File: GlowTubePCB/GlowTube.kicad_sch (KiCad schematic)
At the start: 38 parts, among them J1 Conn_01x07, P1 Solder_Pad, P2 Solder_Pad, P3 Solder_Pad, P4 Solder_Pad, P5 Solder_Pad, P6 Solder_Pad, SW1 TS-1185EC-C-D-B, SW2 TS-1185EC-C-D-B, U1 SN74AHCT32QPWRQ1, U2 ESP32-WROOM-32E (4MB), U3 CP2102-GMR, U4 BL1117-33CX, U5 UMH3N, U6 MSM261D4030H1CPM

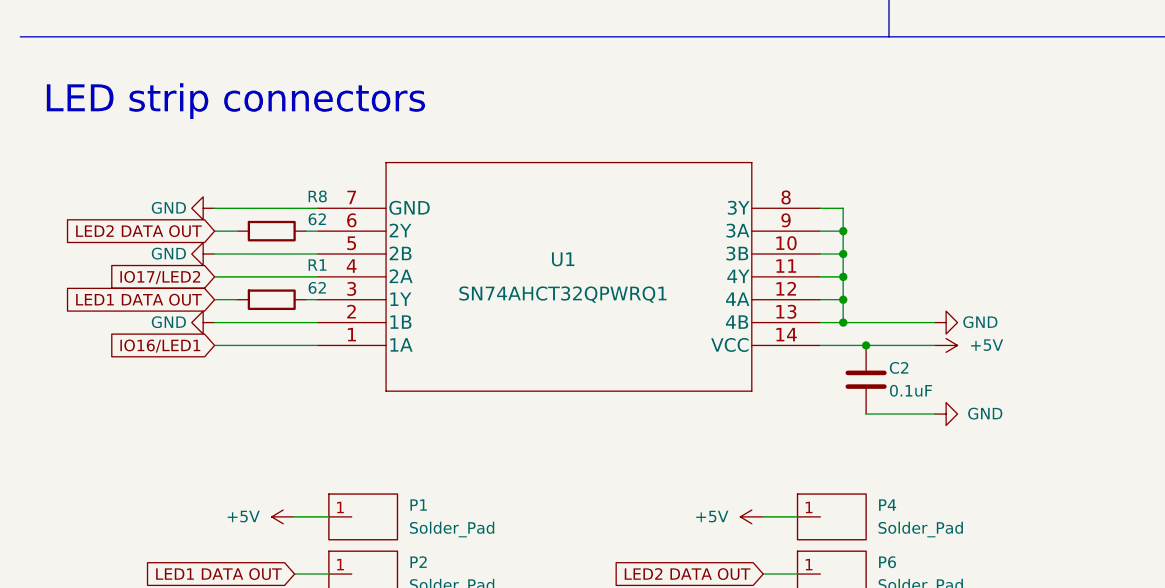
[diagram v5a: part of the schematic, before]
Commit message: replaced microphone and levelshifter
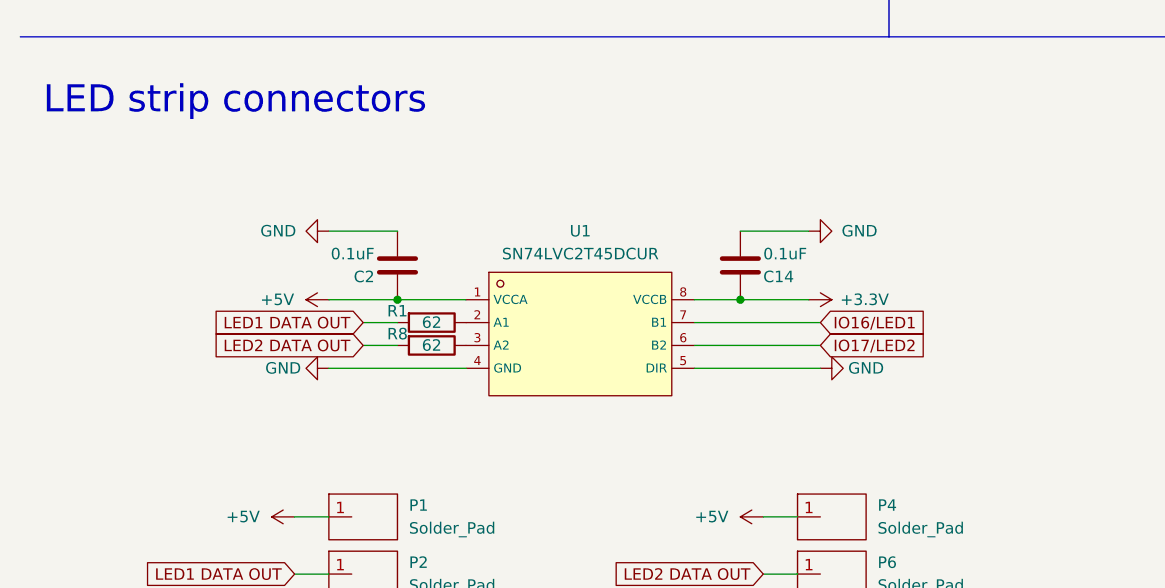
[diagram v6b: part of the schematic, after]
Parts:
- removed U1: SN74AHCT32QPWRQ1, SN74AHCT32QPWRQ1:SN74AHCT32QPWRQ1, symbol SN74AHCT32QPWRQ1:SN74AHCT32QPWRQ1
- added C14: 0.1uF, Capacitor_SMD:C_0603_1608Metric_Pad1.08x0.95mm_HandSolder, symbol Device:C
- added U1: SN74LVC2T45DCUR, footprint:VSSOP-8_L2.4-W2.1-P0.50-LS3.2-BR, symbol MyParts:SN74LVC2T45DCUR
- J1, P1, P2, P3, P4, P5, P6: now left out of the parts list
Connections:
- net +3V3: now also C14.1, U1.8 (VCCB)
- net +5V: now also U1.1 (VCCA)
- net GND: now also C14.2, U1.4 (GND), U1.5 (DIR)
- net IO16/LED1: now also U1.7 (B1)
- net IO17/LED2: now also U1.6 (B2)
- net at R8.1: now also U1.3 (A2)
- net at R1.1: now also U1.2 (A1)

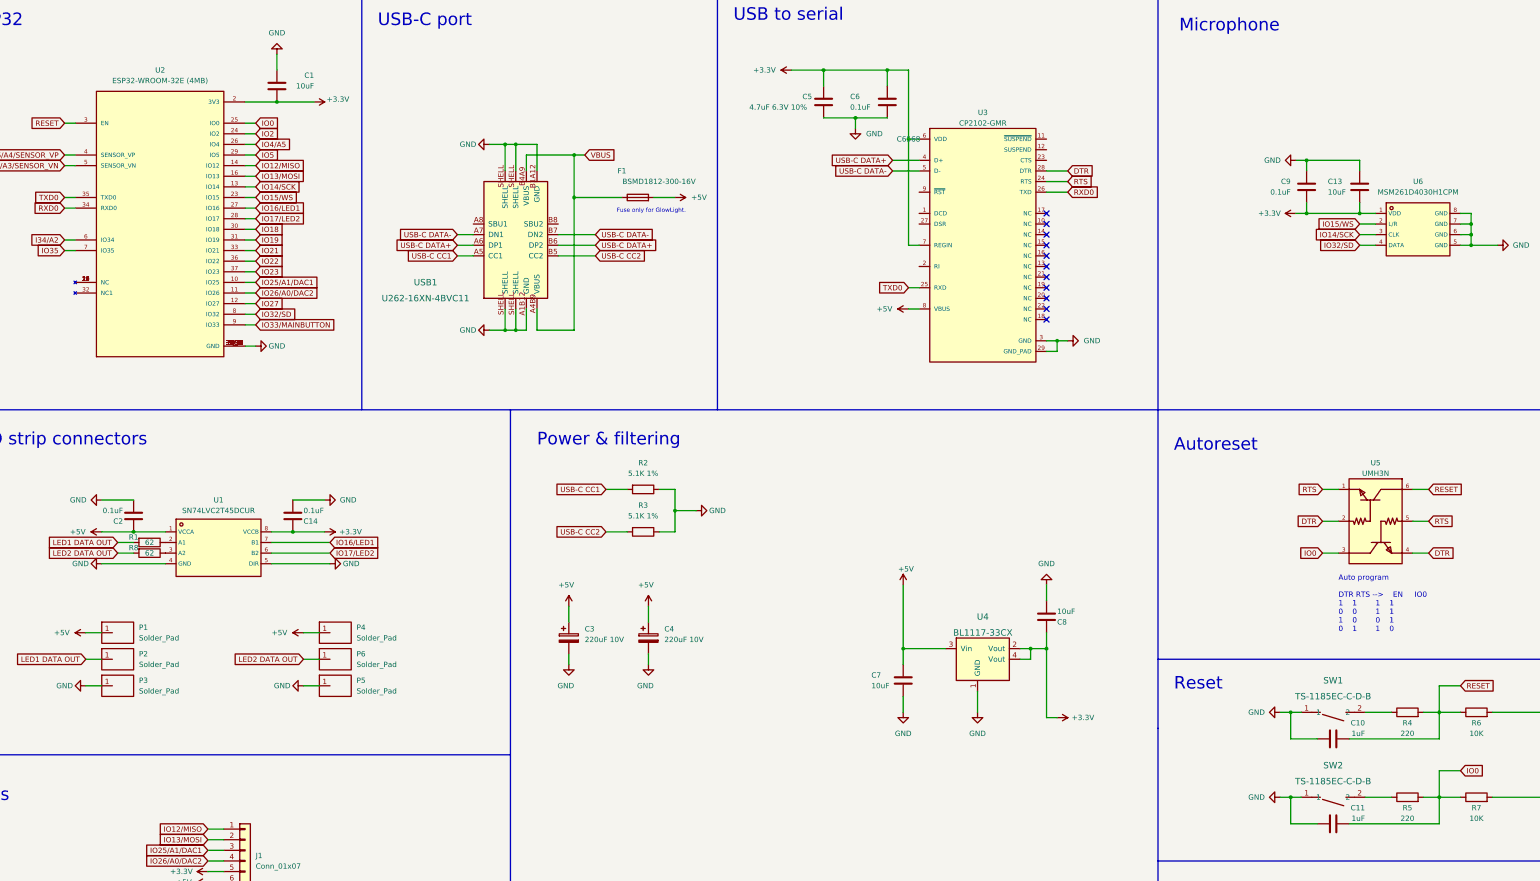
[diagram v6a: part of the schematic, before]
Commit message: updated PCB designs to release candidate 1
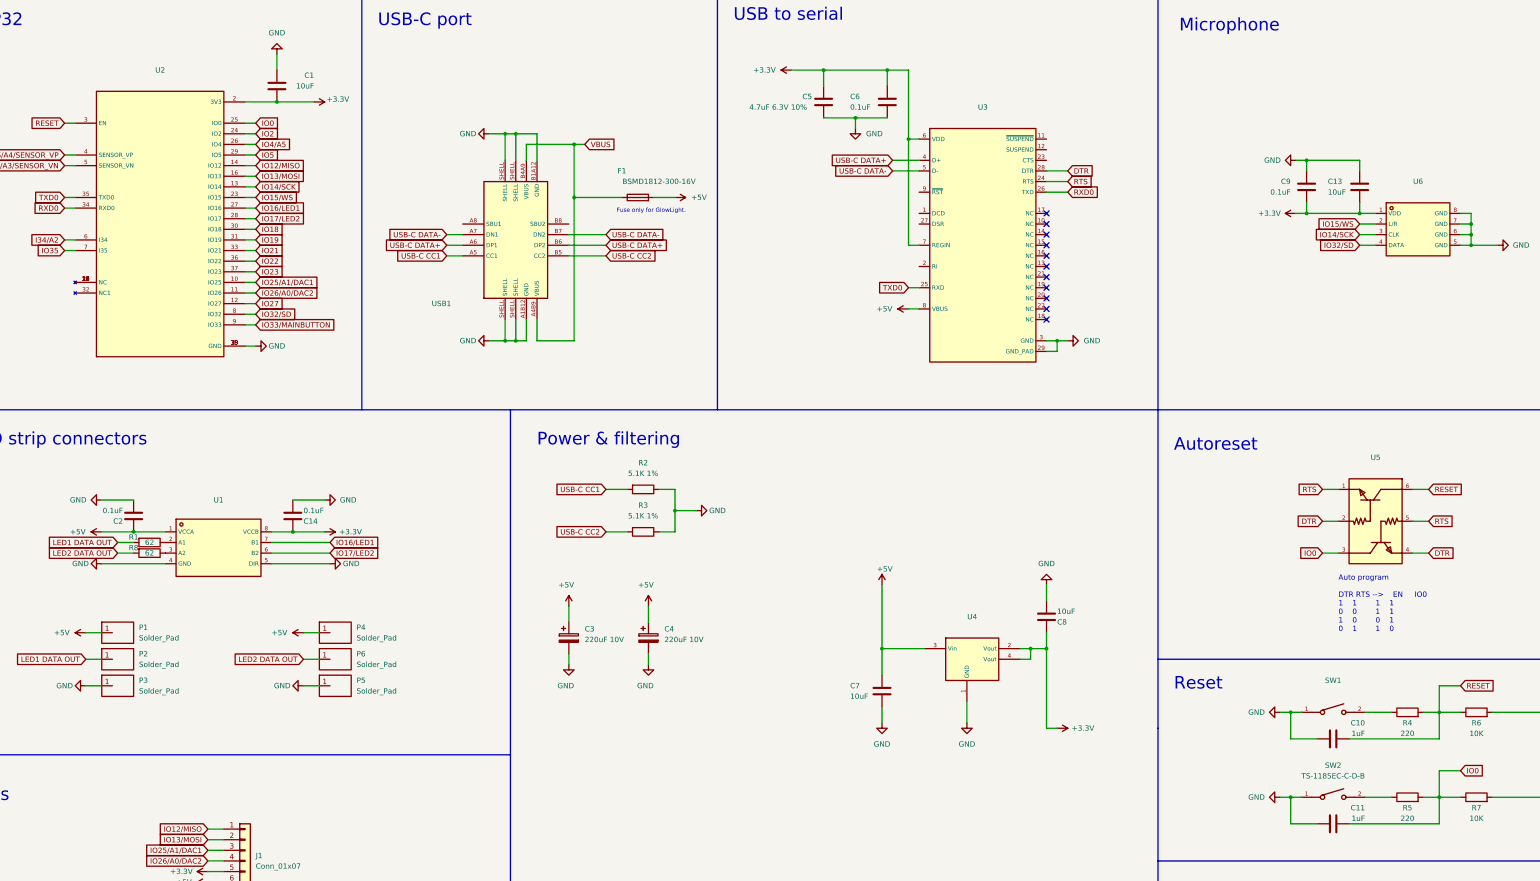
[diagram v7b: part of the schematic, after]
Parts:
- removed SW1, SW2: TS-1185EC-C-D-B, TS-1185EC-C-D-B:TS-1185EC-C-D-B, symbol TS-1185EC-C-D-B:TS-1185EC-C-D-B
- removed U2: ESP32-WROOM-32E (4MB), ESP32-WROOM-32E__16MB_:MODULE_ESP32-WROOM-32E_(16MB), symbol ESP32-WROOM-32E__16MB_:ESP32-WROOM-32E (4MB)
- removed U3: CP2102-GMR, CP2102-GMR:CP2102-GMR, symbol CP2102-GMR:CP2102-GMR
- removed U4: BL1117-33CX, Package_TO_SOT_SMD:SOT-223, symbol BL1117-33CX:BL1117-33CX
- removed U5: UMH3N, footprint:SC-70-6_L2.2-W1.3-P0.65-LS2.1-BR, symbol LCSC:UMH3N
- removed USB1: U262-16XN-4BVC11, U262-161N-4BVC11:USB-3.1-SMD_U262-161N-4BVC11, symbol U262-161N-4BVC11:U262-16XN-4BVC11
- added SW1: (no value), symbol MyParts:TS-1185EC-C-D-B
- added SW2: TS-1185EC-C-D-B, footprint:SW-SMD_4P-L3.7-W3.0-P1.50-LS4.7, symbol MyParts:TS-1185EC-C-D-B
- added U2: (no value), symbol MyParts:ESP32-WROOM-32E
- added U3: (no value), symbol MyParts:CP2102-GMR
- added U4: (no value), symbol MyParts:BL1117-33CX
- added U5: (no value), symbol MyParts:UMH3N
- added USB1: (no value), symbol MyParts:U262-161N-4BVC11
- U1: value SN74LVC2T45DCUR -> (none); footprint footprint:VSSOP-8_L2.4-W2.1-P0.50-LS3.2-BR -> (none)
- U6: value MSM261D4030H1CPM -> (none); footprint footprint:MIC-SMD_8P-L3.0-W4.0-P0.85-BL -> (none); LCSC # (none) -> C966942
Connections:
- net +3V3: now also U2.2 (3V3), U3.6 (VDD), U3.7 (REGIN), U4.2 (Vout), U4.4 (Vout)
- net +5V: now also U3.8 (VBUS), U4.3 (Vin)
- net DTR: now also U3.28 (DTR), U5.2 (B), U5.4 (E)
- net GND: now also SW1.1, SW2.1, U2.1 (GND), U2.15 (GND), U2.38 (GND), U2.39 (GND), U3.29 (GND_PAD), U3.3 (GND), U4.1 (GND), USB1.A1B12 (GND), USB1.B1A12 (GND), USB1.SHELL
- net I34/A2: now also U2.6 (I34)
- net I39/A3/SENSOR_VN: now also U2.5 (SENSOR_VN)
- net IO0: now also U2.25 (IO0), U5.3 (C)
- net IO12/MISO: now also U2.14 (IO12)
- net IO13/MOSI: now also U2.16 (IO13)
- net IO14/SCK: now also U2.13 (IO14)
- net IO15/WS: now also U2.23 (IO15)
- net IO16/LED1: now also U2.27 (IO16)
- net IO17/LED2: now also U2.28 (IO17)
- net IO18: now also U2.30 (IO18)
- net IO19: now also U2.31 (IO19)
- net IO2: now also U2.24 (IO2)
- net IO21: now also U2.33 (IO21)
- net IO22: now also U2.36 (IO22)
- net IO23: now also U2.37 (IO23)
- net IO25/A1/DAC1: now also U2.10 (IO25)
- net IO26/A0/DAC2: now also U2.11 (IO26)
- net IO27: now also U2.12 (IO27)
- net IO32/SD: now also U2.8 (IO32)
- net IO33/MAINBUTTON: now also U2.9 (IO33)
- net IO35: now also U2.7 (I35)
- net IO36/A4/SENSOR_VP: now also U2.4 (SENSOR_VP)
- net IO4/A5: now also U2.26 (IO4)
- net IO5: now also U2.29 (IO5)
- net RESET: now also U2.3 (EN), U5.6 (C)
- net RTS: now also U3.24 (RTS), U5.1 (E), U5.5 (B)
- net RXD0: now also U2.34 (RXD0), U3.26 (TXD)
- net TXD0: now also U2.35 (TXD0), U3.25 (RXD)
- net USB-C CC1: now also USB1.A5 (CC1)
- net USB-C CC2: now also USB1.B5 (CC2)
- net USB-C DATA+: now also U3.4 (D+), USB1.A6 (DP1), USB1.B6 (DP2)
- net USB-C DATA-: now also U3.5 (D-), USB1.A7 (DN1), USB1.B7 (DN2)
- net VBUS: now also USB1.A4B9 (VBUS), USB1.B4A9 (VBUS)
- net at R5.1: now also SW2.2
- net at R4.1: now also SW1.2
- new net: U2.17 (NC), U2.18 (NC), U2.19 (NC), U2.20 (NC), U2.21 (NC), U2.22 (NC)
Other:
- moved on the sheet: C7

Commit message: fixed pcbs
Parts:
- C10, C11: value 1uF -> (none); footprint Capacitor_SMD:C_0603_1608Metric_Pad1.08x0.95mm_HandSolder -> (none); LCSC Part # C1588 -> C15849
- SW1: value (none) -> TS-1185EC-C-D-B; footprint (none) -> footprint:SW-SMD_4P-L3.7-W3.0-P1.50-LS4.7
- U1: value (none) -> SN74LVC2T45DCUR; footprint (none) -> footprint:VSSOP-8_L2.4-W2.1-P0.50-LS3.2-BR
- U2: value (none) -> ESP32-WROOM-32E; footprint (none) -> footprint:WIFI-SMD_ESP32-WROOM-32E
- U3: value (none) -> CP2102-GMR; footprint (none) -> footprint:QFN-28_L5.0-W5.0-P0.50-BL-EP
- U4: value (none) -> BL1117-33CX; footprint (none) -> footprint:SOT-223-4_L6.5-W3.5-P2.30-LS7.0-BR
- U5: value (none) -> UMH3N; footprint (none) -> footprint:SC-70-6_L2.2-W1.3-P0.65-LS2.1-BR
- U6: value (none) -> MSM261D4030H1CPM; footprint (none) -> footprint:MIC-SMD_8P-L3.0-W4.0-P0.85-BL
- USB1: value (none) -> U262-161N-4BVC11; footprint (none) -> footprint:USB-3.1-SMD_U262-161N-4BVC11
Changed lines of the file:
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@@
       (effects (font (size 1.27 1.27)) (justify right))
     )
-    (property "Value" "1uF" (id 1) (at 349.25 209.55 90)
-      (effects (font (size 1.27 1.27)) (justify right))
-    )
-    (property "Footprint" "Capacitor_SMD:C_0603_1608Metric_Pad1.08x0.95mm_HandSolder" (id 2) (at 309.88 210.82 0)
+    (property "Value" "" (id 1) (at 349.25 209.55 90)
+      (effects (font (size 1.27 1.27)) (justify right))
+    )
+    (property "Footprint" "" (id 2) (at 309.88 210.82 0)
       (effects (font (size 1.27 1.27)) hide)
     )
@@
       (effects (font (size 1.27 1.27)) hide)
     )
-    (property "LCSC Part #" "C1588" (id 6) (at 330.2 213.36 0)
+    (property "LCSC Part #" "C15849" (id 6) (at 330.2 213.36 0)
       (effects (font (size 1.27 1.27)) hide)
     )
@@
     (in_bom yes) (on_board yes) (fields_autoplaced)
     (property "Reference" "U3" (id 0) (at 257.81 39.37 0))
-    (property "Value" "" (id 1) (at 257.81 41.91 0))
-    (property "Footprint" "" (id 2) (at 259.08 104.14 0)
+    (property "Value" "CP2102-GMR" (id 1) (at 257.81 41.91 0))
+    (property "Footprint" "footprint:QFN-28_L5.0-W5.0-P0.50-BL-EP" (id 2) (at 259.08 104.14 0)
       (effects (font (size 1.27 1.27) italic) hide)
     )
@@
     (in_bom yes) (on_board yes) (fields_autoplaced)
     (property "Reference" "U2" (id 0) (at 60.96 30.48 0))
-    (property "Value" "" (id 1) (at 60.96 33.02 0))
-    (property "Footprint" "" (id 2) (at 60.96 107.95 0)
+    (property "Value" "ESP32-WROOM-32E" (id 1) (at 60.96 33.02 0))
+    (property "Footprint" "footprint:WIFI-SMD_ESP32-WROOM-32E" (id 2) (at 60.96 107.95 0)
       (effects (font (size 1.27 1.27) italic) hide)
     )
@@
     (in_bom yes) (on_board yes) (fields_autoplaced)
     (property "Reference" "U4" (id 0) (at 255.27 161.29 0))
-    (property "Value" "" (id 1) (at 255.27 163.83 0))
-    (property "Footprint" "" (id 2) (at 255.27 170.18 0)
+    (property "Value" "BL1117-33CX" (id 1) (at 255.27 163.83 0))
+    (property "Footprint" "footprint:SOT-223-4_L6.5-W3.5-P2.30-LS7.0-BR" (id 2) (at 255.27 170.18 0)
       (effects (font (size 1.27 1.27) italic) hide)
     )
@@
     (in_bom yes) (on_board yes) (fields_autoplaced)
     (property "Reference" "U6" (id 0) (at 361.95 57.15 0))
-    (property "Value" "" (id 1) (at 361.95 59.69 0))
-    (property "Footprint" "" (id 2) (at 361.95 66.04 0)
+    (property "Value" "MSM261D4030H1CPM" (id 1) (at 361.95 59.69 0))
+    (property "Footprint" "footprint:MIC-SMD_8P-L3.0-W4.0-P0.85-BL" (id 2) (at 361.95 66.04 0)
       (effects (font (size 1.27 1.27) italic) hide)
     )
@@
     (in_bom yes) (on_board yes) (fields_autoplaced)
     (property "Reference" "U1" (id 0) (at 74.93 133.35 0))
-    (property "Value" "" (id 1) (at 74.93 135.89 0))
-    (property "Footprint" "" (id 2) (at 74.93 135.89 0)
+    (property "Value" "SN74LVC2T45DCUR" (id 1) (at 74.93 135.89 0))
+    (property "Footprint" "footprint:VSSOP-8_L2.4-W2.1-P0.50-LS3.2-BR" (id 2) (at 74.93 135.89 0)
       (effects (font (size 1.27 1.27) italic) hide)
     )
@@
     (in_bom yes) (on_board yes) (fields_autoplaced)
     (property "Reference" "U5" (id 0) (at 351.79 123.19 0))
-    (property "Value" "" (id 1) (at 351.79 125.73 0))
-    (property "Footprint" "" (id 2) (at 351.79 151.13 0)
+    (property "Value" "UMH3N" (id 1) (at 351.79 125.73 0))
+    (property "Footprint" "footprint:SC-70-6_L2.2-W1.3-P0.65-LS2.1-BR" (id 2) (at 351.79 151.13 0)
       (effects (font (size 1.27 1.27) italic) hide)
     )
@@
     (in_bom yes) (on_board yes) (fields_autoplaced)
     (property "Reference" "SW1" (id 0) (at 341.63 176.53 0))
-    (property "Value" "" (id 1) (at 341.63 179.07 0))
-    (property "Footprint" "" (id 2) (at 342.9 191.77 0)
+    (property "Value" "TS-1185EC-C-D-B" (id 1) (at 341.63 179.07 0))
+    (property "Footprint" "footprint:SW-SMD_4P-L3.7-W3.0-P1.50-LS4.7" (id 2) (at 342.9 191.77 0)
       (effects (font (size 1.27 1.27) italic) hide)
     )
@@
       (effects (font (size 1.27 1.27)) (justify right))
     )
-    (property "Value" "1uF" (id 1) (at 349.25 189.23 90)
-      (effects (font (size 1.27 1.27)) (justify right))
-    )
-    (property "Footprint" "Capacitor_SMD:C_0603_1608Metric_Pad1.08x0.95mm_HandSolder" (id 2) (at 309.88 190.5 0)
+    (property "Value" "" (id 1) (at 349.25 189.23 90)
+      (effects (font (size 1.27 1.27)) (justify right))
+    )
+    (property "Footprint" "" (id 2) (at 309.88 190.5 0)
       (effects (font (size 1.27 1.27)) hide)
     )
@@
       (effects (font (size 1.27 1.27)) hide)
     )
-    (property "LCSC Part #" "C1588" (id 6) (at 330.2 193.04 0)
+    (property "LCSC Part #" "C15849" (id 6) (at 330.2 193.04 0)
       (effects (font (size 1.27 1.27)) hide)
     )
@@
     (in_bom yes) (on_board yes)
     (property "Reference" "USB1" (id 0) (at 128.27 86.36 90))
-    (property "Value" "" (id 1) (at 128.27 88.9 90))
-    (property "Footprint" "" (id 2) (at 170.18 68.58 0)
+    (property "Value" "U262-161N-4BVC11" (id 1) (at 128.27 88.9 90))
+    (property "Footprint" "footprint:USB-3.1-SMD_U262-161N-4BVC11" (id 2) (at 170.18 68.58 0)
       (effects (font (size 1.27 1.27) italic) hide)
     )
